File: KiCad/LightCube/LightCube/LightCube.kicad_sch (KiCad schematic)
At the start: 10 parts, among them SW1 KCD11, U1 TP4056, U2 MPU-6050_breakout, U3 BoostConverter_MT3608_Breakout, U4 WeMos_D1_mini

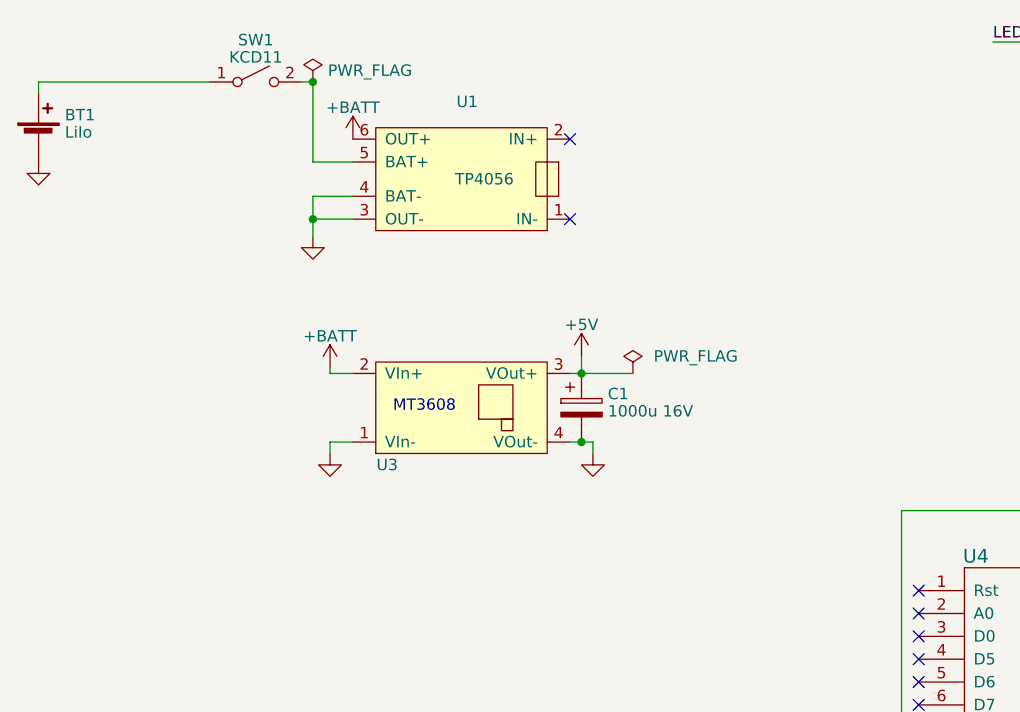
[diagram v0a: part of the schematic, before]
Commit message: Modified some light effects.
Limited brightness due to MT3608 overload and TP4056 overcurrent protection.
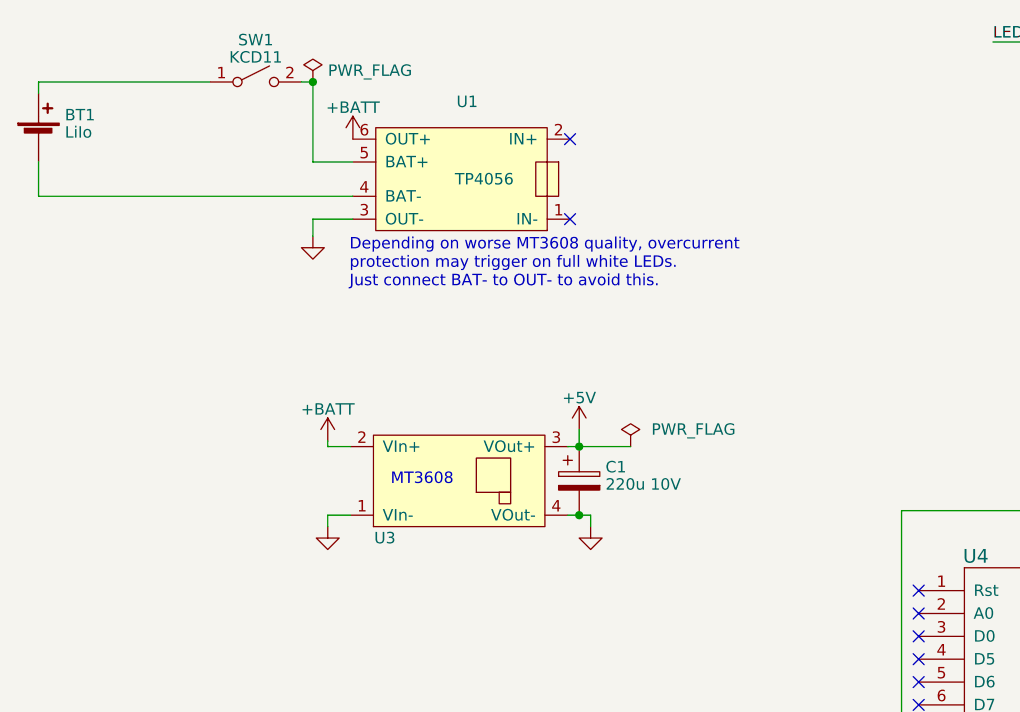
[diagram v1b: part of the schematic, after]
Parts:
- C1: value 1000u 16V -> 220u 10V
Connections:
- net GND: no longer BT1.2 (-), U1.4 (BAT-)
- new net: BT1.2 (-), U1.4 (BAT-)
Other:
- note added: "Depending on worse MT3608 quality, overcurrent protection may trigger on full white LEDs. Just connect BAT- to OUT- to avoid this."
- moved on the sheet: C1, U3
